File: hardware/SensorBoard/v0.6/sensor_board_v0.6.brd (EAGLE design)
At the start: 46.8 x 39.9 mm, 48 parts, among them J3 USB-MICROB, U1 ATMEGA328P, U10 CCS811, U11 RFM69HW, U2 TSL2561, U4 MPL115A, U5 FT231XS, U7 SHT31, U8 MCP1703/3.3V, U9 MCP1703CB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

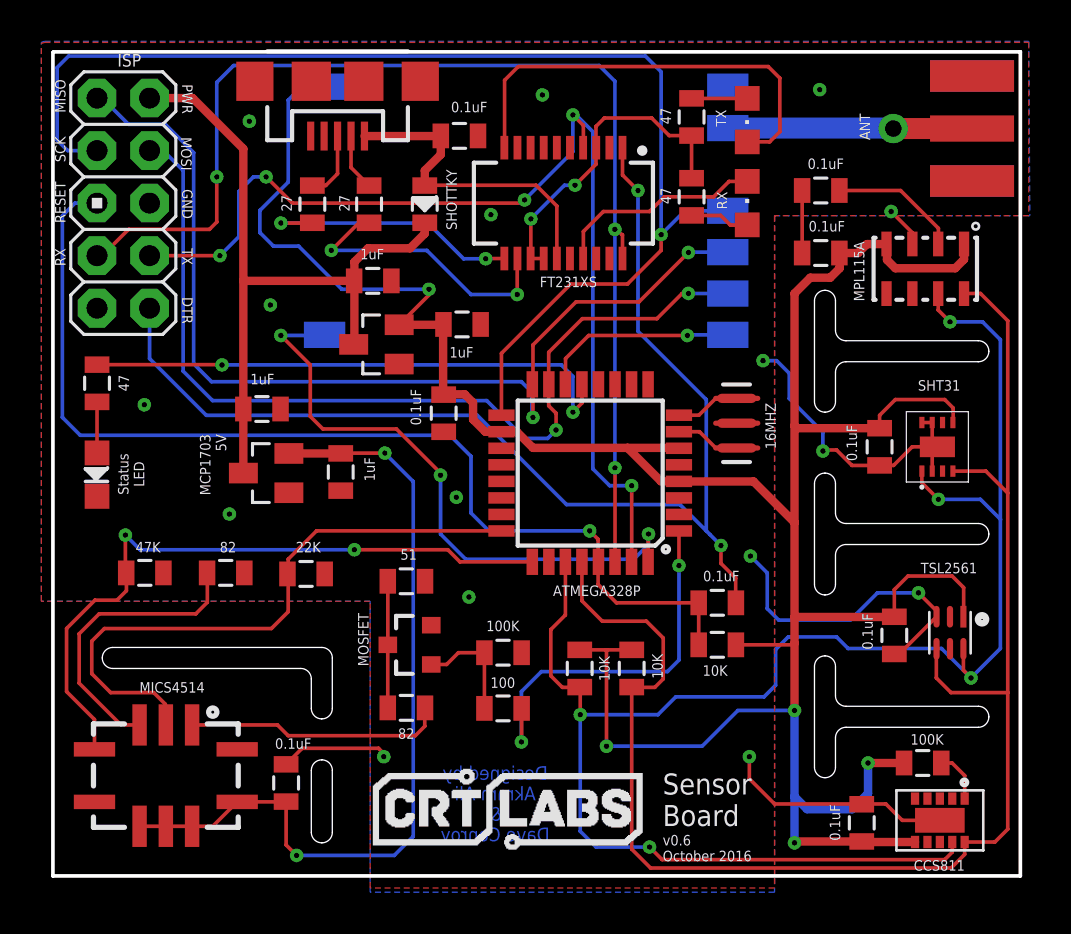
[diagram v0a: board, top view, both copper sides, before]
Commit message: I2C pullups silkscreen
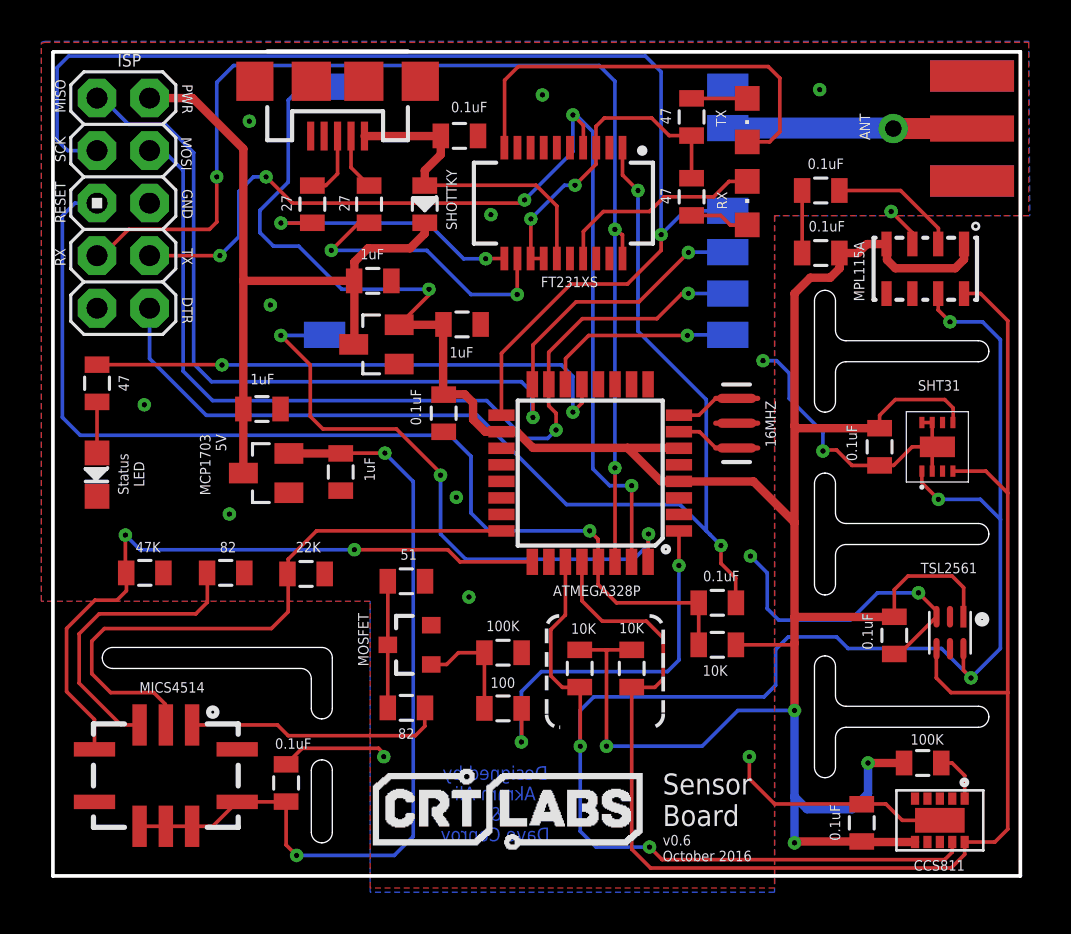
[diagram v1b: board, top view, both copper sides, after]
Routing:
- net SDA: track 83.9 -> 85.5 mm
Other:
- board text added: "I2C Pullups"
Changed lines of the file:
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@@
 <text x="51.9176" y="35.9664" size="0.508" layer="118" font="vector" rot="R90" align="bottom-center">AIr Pressure</text>
 <text x="11.43" y="7.5184" size="0.508" layer="118" font="vector" rot="R180" align="bottom-center">CO / NO2</text>
+<wire x1="30.3784" y1="19.2024" x2="29.7688" y2="18.5928" width="0.1778" layer="121" style="dashdot" curve="90"/>
+<wire x1="29.7688" y1="18.5928" x2="29.7688" y2="14.4272" width="0.1778" layer="121" style="dashdot"/>
+<wire x1="34.7472" y1="19.2024" x2="35.4076" y2="18.542" width="0.1778" layer="121" style="dashdot" curve="-90"/>
+<wire x1="35.4076" y1="18.542" x2="35.4076" y2="14.5288" width="0.1778" layer="121" style="dashdot"/>
+<wire x1="29.7688" y1="14.4272" x2="30.3784" y2="13.8176" width="0.1778" layer="121" style="dashdot" curve="90"/>
+<wire x1="30.3784" y1="13.8176" x2="30.4292" y2="13.8176" width="0.1778" layer="121" style="dashdot"/>
+<wire x1="35.4076" y1="14.478" x2="35.4076" y2="14.4272" width="0.1778" layer="121" style="dashdot"/>
+<wire x1="35.4076" y1="14.4272" x2="34.798" y2="13.8176" width="0.1778" layer="121" style="dashdot" curve="-90"/>
+<text x="32.6644" y="14.8844" size="0.508" layer="118" font="vector" rot="R180" align="bottom-center">I2C Pullups</text>
 </plain>
 <attributes>
@@
 <attribute name="MF" value="" x="31.369" y="16.6624" size="1.778" layer="27" rot="R90" display="off"/>
 <attribute name="MPN" value="" x="31.369" y="16.6624" size="1.778" layer="27" rot="R90" display="off"/>
-<attribute name="VALUE" x="32.8168" y="16.0528" size="0.508" layer="121" font="vector" rot="R90"/>
+<attribute name="VALUE" x="32.1564" y="18.8468" size="0.508" layer="121" font="vector" rot="R180"/>
 </element>
 <element name="R6" library="SparkFun-Resistors" package="0805" value="10K" x="33.8836" y="16.6624" smashed="yes" rot="R90">
@@
 <attribute name="MF" value="" x="33.8836" y="16.6624" size="1.778" layer="27" rot="R90" display="off"/>
 <attribute name="MPN" value="" x="33.8836" y="16.6624" size="1.778" layer="27" rot="R90" display="off"/>
-<attribute name="VALUE" x="34.8742" y="17.3736" size="0.508" layer="121" font="vector" rot="R270"/>
+<attribute name="VALUE" x="33.274" y="18.3642" size="0.508" layer="121" font="vector"/>
 </element>
 <element name="C3" library="SparkFun-Passives" package="0805" value="0.1uF" x="46.5836" y="18.2626" smashed="yes" rot="R270">
@@
 <attribute name="MF" value="" x="38.9636" y="28.5242" size="1.778" layer="27" rot="R90" display="off"/>
 <attribute name="MPN" value="" x="38.9636" y="28.5242" size="1.778" layer="27" rot="R90" display="off"/>
-<attribute name="VALUE" x="40.8559" y="27.2669" size="0.508" layer="121" font="vector" rot="R90"/>
+<attribute name="VALUE" x="40.8559" y="27.3685" size="0.508" layer="121" font="vector" rot="R90"/>
 </element>
 <element name="LED2" library="adafruit" package="CHIPLED_0805" value="" x="8.0264" y="26.035" smashed="yes" rot="R180">
@@
 <element name="U5" library="SparkFun-DigitalIC" package="SSOP20_L" value="FT231XS" x="30.5816" y="39.1668" smashed="yes" rot="R180">
 <attribute name="PROD_ID" value="IC-11524" x="30.5816" y="39.1668" size="1.778" layer="27" rot="R180" display="off"/>
-<attribute name="VALUE" x="32.2072" y="35.6108" size="0.508" layer="121" font="vector" rot="R180"/>
+<attribute name="VALUE" x="32.258" y="35.6108" size="0.508" layer="121" font="vector" rot="R180"/>
 </element>
 <element name="RX" library="adafruit" package="CHIPLED_0805" value="Green" x="39.4716" y="39.1668" smashed="yes">
@@
 </element>
 <element name="U11" library="RFM69 USB Gateway" package="LOWPOWERLAB_RFM69W-MINPADS" value="RFM69HW" x="30.5308" y="37.7952" smashed="yes" rot="MR180">
-<attribute name="VALUE" x="30.488" y="30.9512" size="0.508" layer="122" font="vector" rot="MR0"/>
+<attribute name="VALUE" x="40.5016" y="36.1616" size="0.508" layer="122" font="vector" rot="MR90"/>
 </element>
 <element name="X1" library="adafruit" package="SMA_EDGELAUNCH" value="" x="52.3748" y="42.7736" smashed="yes" rot="R180">
@@
 <wire x1="34.7472" y1="8.0264" x2="32.1564" y2="8.0264" width="0.1778" layer="16"/>
 <wire x1="32.1564" y1="8.0264" x2="31.3944" y2="8.7884" width="0.1778" layer="16"/>
-<wire x1="31.3944" y1="8.7884" x2="31.3944" y2="14.4272" width="0.1778" layer="16"/>
-<via x="31.3944" y="14.4272" extent="1-16" drill="0.254" diameter="0.127"/>
-<wire x1="31.3944" y1="14.4272" x2="31.3944" y2="15.737" width="0.1778" layer="1"/>
+<via x="31.3944" y="12.9032" extent="1-16" drill="0.254" diameter="0.127"/>
 <wire x1="31.3944" y1="15.737" x2="31.369" y2="15.7624" width="0.1778" layer="1"/>
 <via x="50.292" y="16.2052" extent="1-16" drill="0.254" diameter="0.127"/>
@@
 <wire x1="40.8432" y1="17.5768" x2="40.8432" y2="15.8496" width="0.1778" layer="16"/>
 <wire x1="40.8432" y1="15.8496" x2="40.2844" y2="15.2908" width="0.1778" layer="16"/>
-<wire x1="40.2844" y1="15.2908" x2="36.0172" y2="15.2908" width="0.1778" layer="16"/>
-<wire x1="36.0172" y1="15.2908" x2="35.1536" y2="14.4272" width="0.1778" layer="16"/>
-<wire x1="35.1536" y1="14.4272" x2="31.3944" y2="14.4272" width="0.1778" layer="16"/>
+<wire x1="40.2844" y1="15.2908" x2="32.0548" y2="15.2908" width="0.1778" layer="16"/>
 <wire x1="51.7144" y1="17.6276" x2="50.292" y2="16.2052" width="0.1778" layer="16"/>
 <wire x1="49.926" y1="17.6146" x2="49.926" y2="16.5712" width="0.1778" layer="1"/>
@@
 <wire x1="44.3484" y1="17.6276" x2="48.8696" y2="17.6276" width="0.1778" layer="16"/>
 <wire x1="48.8696" y1="17.6276" x2="50.292" y2="16.2052" width="0.1778" layer="16"/>
+<wire x1="31.3944" y1="15.737" x2="31.3944" y2="12.9032" width="0.1778" layer="1"/>
+<wire x1="31.3944" y1="8.7884" x2="31.3944" y2="12.9032" width="0.1778" layer="16"/>
+<wire x1="32.0548" y1="15.2908" x2="31.3944" y2="14.6304" width="0.1778" layer="16"/>
+<wire x1="31.3944" y1="14.6304" x2="31.3944" y2="12.9032" width="0.1778" layer="16"/>
 </signal>
 <signal name="D5">
